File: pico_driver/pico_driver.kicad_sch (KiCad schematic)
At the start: 6 parts, among them J1 GPIO, U1 CAT24C256

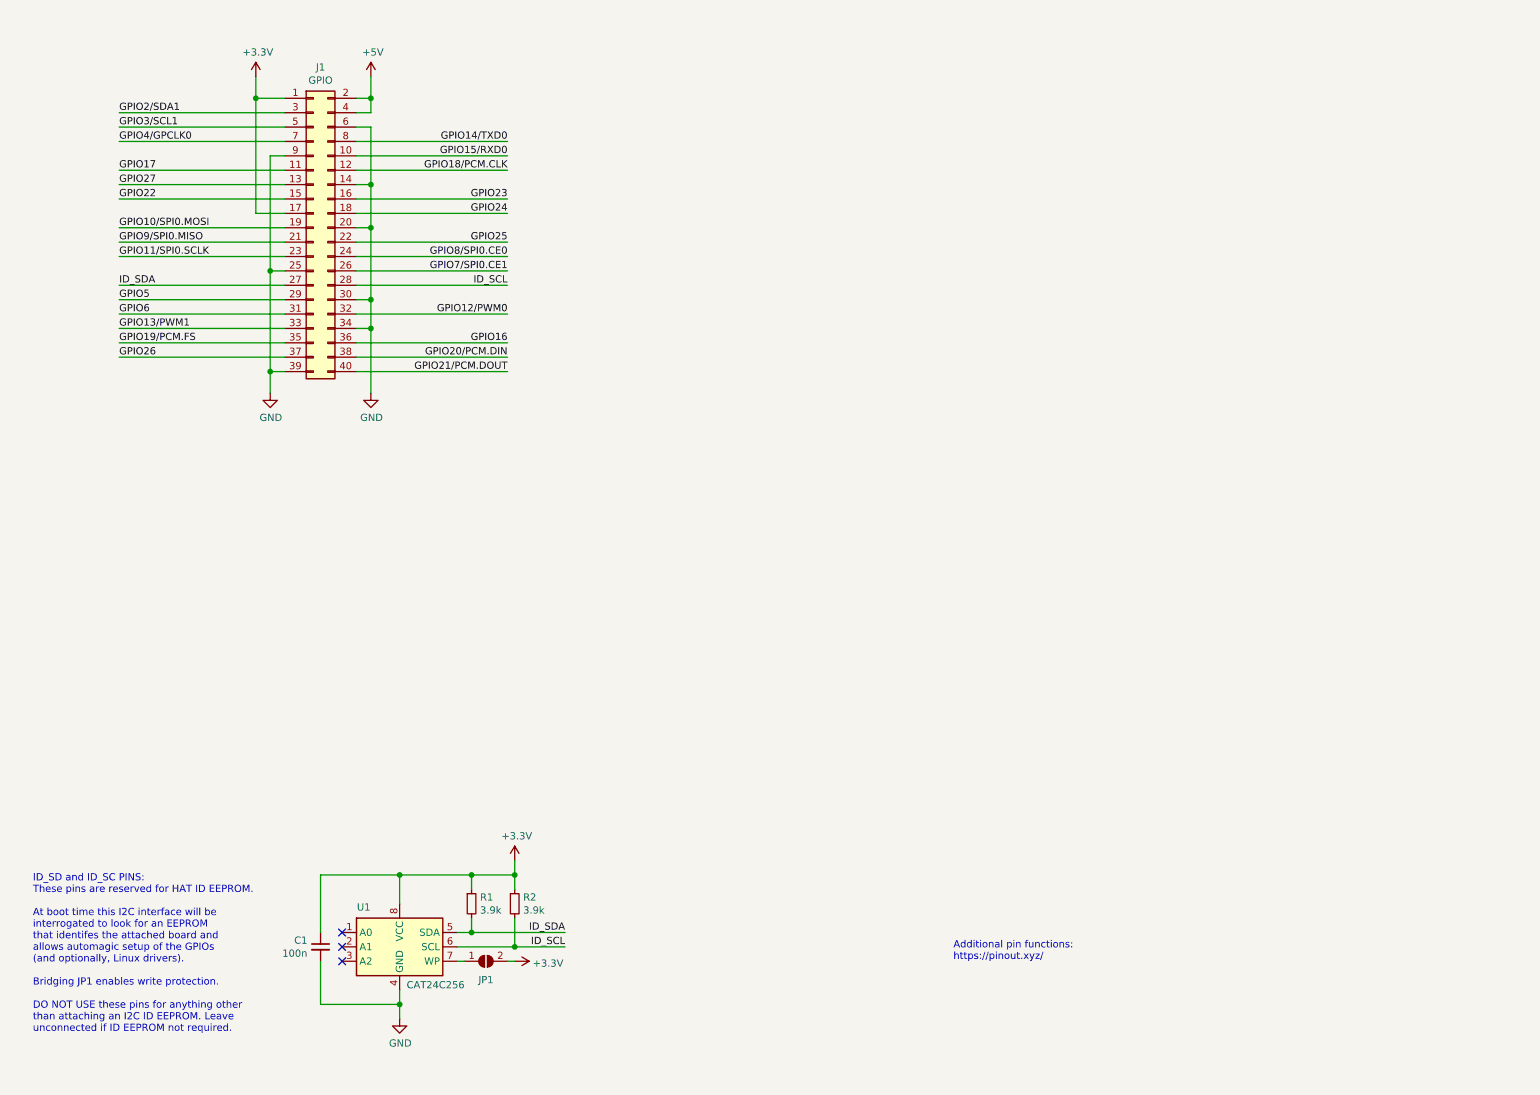
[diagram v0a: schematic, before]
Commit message: update schematic
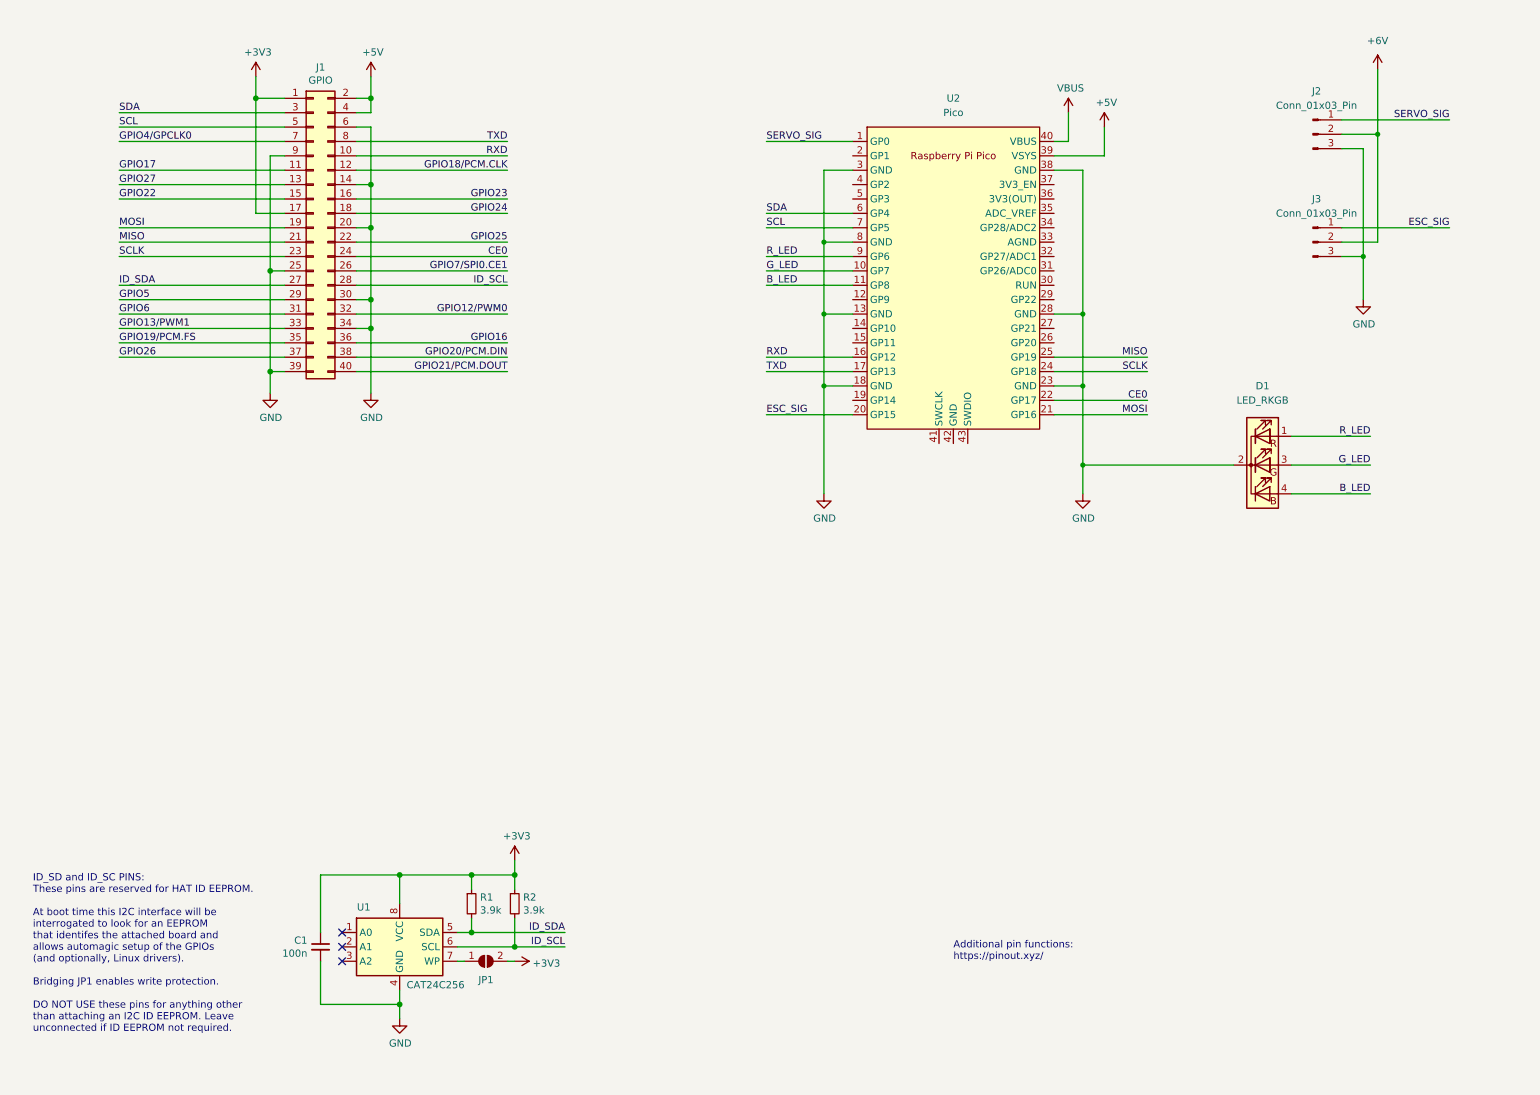
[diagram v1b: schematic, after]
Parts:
- added D1: LED_RKGB, symbol Device:LED_RKGB
- added J2, J3: Conn_01x03_Pin, symbol Connector:Conn_01x03_Pin
- added U2: Pico, RPi_Pico:RPi_Pico_SMD_TH, symbol Pico:Pico
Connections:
- net +5V: now also U2.39 (VSYS)
- net GND: now also D1.2 (K), J2.3 (Pin_3), J3.3 (Pin_3), U2.13 (GND), U2.18 (GND), U2.23 (GND), U2.28 (GND), U2.3 (GND), U2.38 (GND), U2.8 (GND)
- net GPIO10/SPI0.MOSI renamed MOSI
- net MOSI: now also U2.21 (GP16)
- net GPIO11/SPI0.SCLK renamed SCLK
- net SCLK: now also U2.24 (GP18)
- net GPIO14/TXD0 renamed TXD
- net TXD: now also U2.17 (GP13)
- net GPIO15/RXD0 renamed RXD
- net RXD: now also U2.16 (GP12)
- net GPIO2/SDA1 renamed SDA
- net SDA: now also U2.6 (GP4)
- net GPIO3/SCL1 renamed SCL
- net SCL: now also U2.7 (GP5)
- net GPIO8/SPI0.CE0 renamed CE0
- net CE0: now also U2.22 (GP17)
- net GPIO9/SPI0.MISO renamed MISO
- net MISO: now also U2.25 (GP19)
- new net +6V: J2.2 (Pin_2), J3.2 (Pin_2)
- new net B_LED: D1.4 (BA), U2.11 (GP8)
- new net ESC_SIG: J3.1 (Pin_1), U2.20 (GP15)
- new net G_LED: D1.3 (GA), U2.10 (GP7)
- new net R_LED: D1.1 (RA), U2.9 (GP6)
- new net SERVO_SIG: J2.1 (Pin_1), U2.1 (GP0)
- new net VBUS: U2.40 (VBUS)

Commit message: update design
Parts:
- added J4: Conn_01x12_Pin, Connector_PinHeader_2.54mm:PinHeader_1x12_P2.54mm_Vertical, symbol Connector:Conn_01x12_Pin
- added J5: PICO_5VOUT, Connector_PinHeader_2.54mm:PinHeader_1x02_P2.54mm_Vertical, symbol Connector:Conn_01x02_Pin
- added R3, R4, R5: 220R, Resistor_SMD:R_1206_3216Metric_Pad1.30x1.75mm_HandSolder, symbol Device:R
- added SW1: SW_SPDT, Button_Switch_THT:SW_E-Switch_EG1271_SPDT, symbol Switch:SW_SPDT
- added SW2: SW_PU, Button_Switch_THT:SW_PUSH_6mm_H5mm, symbol Switch:SW_SPST
- added SW3: SW_PD, Button_Switch_THT:SW_PUSH_6mm_H5mm, symbol Switch:SW_SPST
- C1: footprint (none) -> Capacitor_SMD:C_0805_2012Metric
- D1: footprint (none) -> LED_THT:LED_D5.0mm-4_RGB
- J2: value Conn_01x03_Pin -> Conn_SERVO; footprint (none) -> Connector_PinHeader_2.54mm:PinHeader_1x03_P2.54mm_Vertical
- J3: value Conn_01x03_Pin -> Conn_ESC; footprint (none) -> Connector_PinHeader_2.54mm:PinHeader_1x03_P2.54mm_Vertical
- JP1: footprint (none) -> Jumper:SolderJumper-2_P1.3mm_Bridged_Pad1.0x1.5mm
- R1, R2: footprint (none) -> Resistor_SMD:R_1206_3216Metric
- U1: footprint (none) -> CAT24C256:TSSOP8_4P50X3P10_ONS
- U2: footprint RPi_Pico:RPi_Pico_SMD_TH -> Pico:RPi_Pico_SMD_TH
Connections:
- net +5V: now also SW1.1 (A); no longer U2.39 (VSYS)
- net B_LED: now also U2.26 (GP20), R5.2; no longer D1.4 (BA), U2.11 (GP8)
- net CE0: now also U2.17 (GP13); no longer U2.22 (GP17)
- net ESC_SIG: now also U2.21 (GP16); no longer U2.20 (GP15)
- net GND: now also U2.33 (AGND), J5.2 (Pin_2), SW3.2 (B)
- net G_LED: now also U2.25 (GP19), R4.2; no longer D1.3 (GA), U2.10 (GP7)
- net MISO: now also U2.15 (GP11); no longer U2.25 (GP19)
- net MOSI: now also U2.16 (GP12); no longer U2.21 (GP16)
- net RXD: now also U2.11 (GP8); no longer U2.16 (GP12)
- net R_LED: now also U2.24 (GP18), R3.2; no longer D1.1 (RA), U2.9 (GP6)
- net SCL: now also U2.20 (GP15); no longer U2.7 (GP5)
- net SCLK: now also U2.14 (GP10); no longer U2.24 (GP18)
- net SDA: now also U2.19 (GP14); no longer U2.6 (GP4)
- net SERVO_SIG: now also U2.27 (GP21); no longer U2.1 (GP0)
- net TXD: now also U2.12 (GP9); no longer U2.17 (GP13)
- net VBUS: now also J5.1 (Pin_1)
- net GP1: now reaches U2.2 (GP1)
- net GP1: now also J4.2 (Pin_2)
- net GP22: now reaches U2.29 (GP22)
- net GP22: now also J4.10 (Pin_10)
- net at U2.31 (GP26/ADC0): now also SW2.1 (A)
- net at U2.32 (GP27/ADC1): now also SW3.1 (A)
- net GP28: now reaches U2.34 (GP28/ADC2)
- net GP28: now also J4.11 (Pin_11)
- net ADC_VREF: now reaches U2.35 (ADC_VREF)
- net ADC_VREF: now also J4.12 (Pin_12)
- net +3V3_PICO: now reaches U2.36 (3V3(OUT))
- net +3V3_PICO: now also SW2.2 (B)
- net GP2: now reaches U2.4 (GP2)
- net GP2: now also J4.3 (Pin_3)
- net GP3: now reaches U2.5 (GP3)
- net GP3: now also J4.4 (Pin_4)
- net +6V renamed VBEC
- new net: D1.4 (BA), R5.1
- new net: D1.3 (GA), R4.1
- new net: D1.1 (RA), R3.1
- new net GP0: J4.1 (Pin_1), U2.1 (GP0)
- new net GP17: J4.9 (Pin_9), U2.22 (GP17)
- new net GP4: J4.5 (Pin_5), U2.6 (GP4)
- new net GP5: J4.6 (Pin_6), U2.7 (GP5)
- new net GP6: J4.7 (Pin_7), U2.9 (GP6)
- new net GP7: J4.8 (Pin_8), U2.10 (GP7)
- new net VSYS: SW1.2 (B), U2.39 (VSYS)
- no-connect marks 3 -> 7
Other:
- moved on the sheet: J2, J3

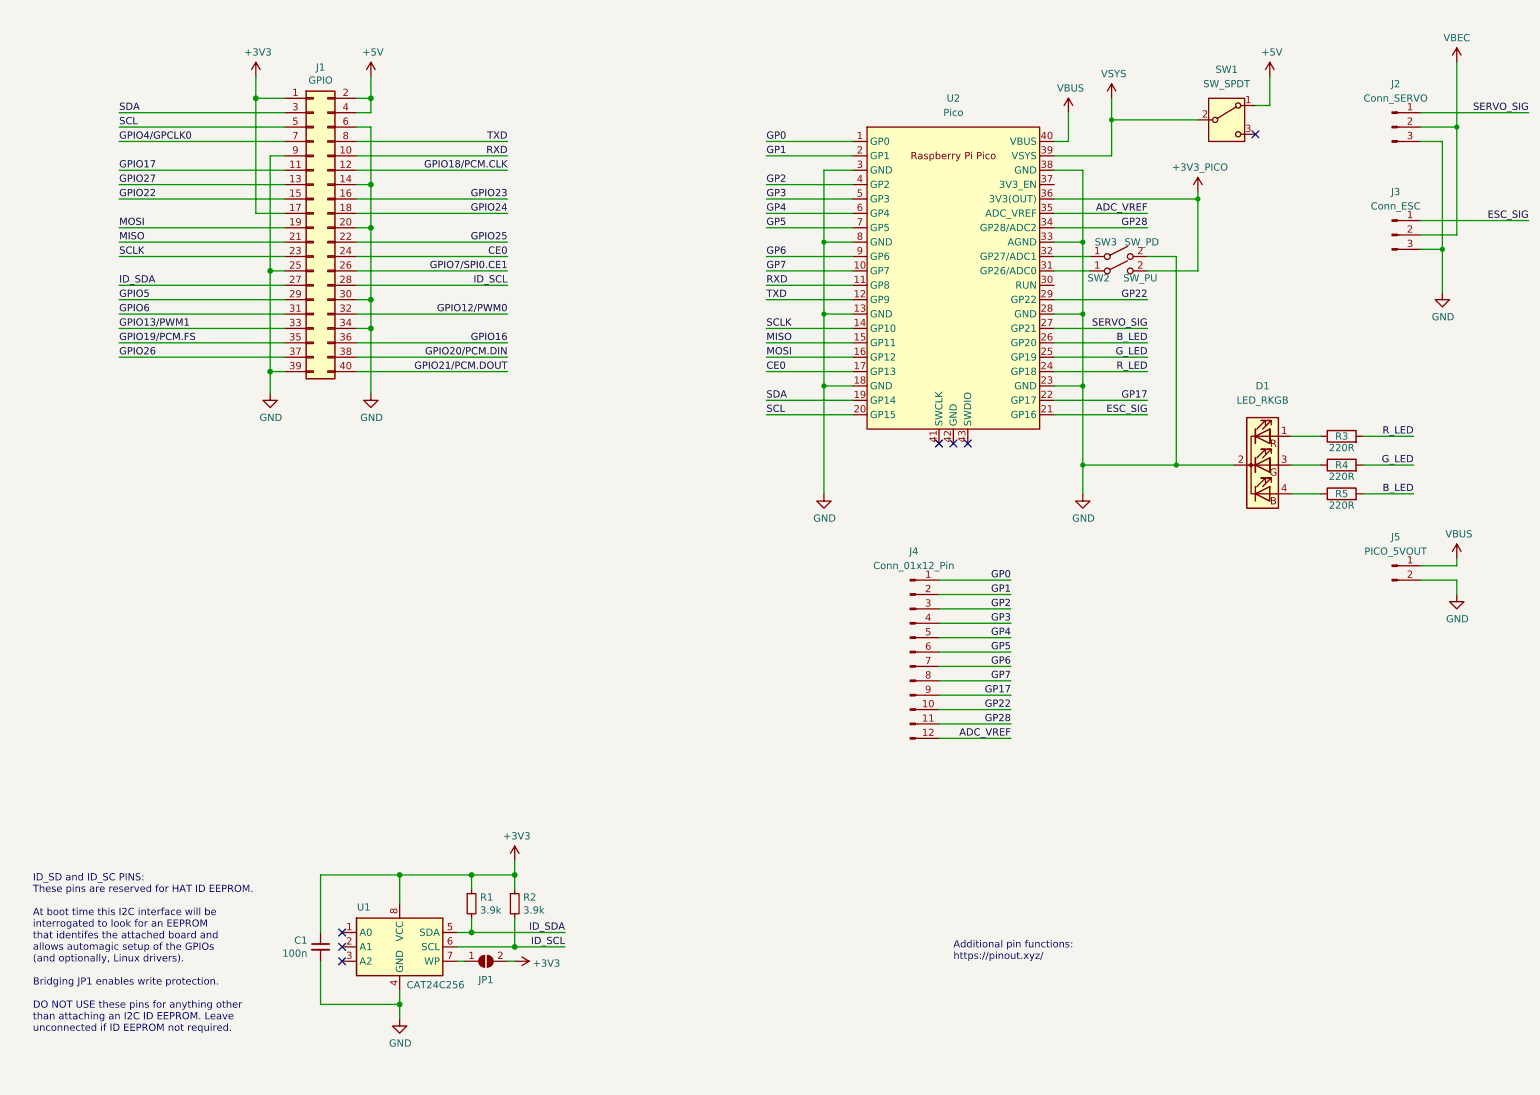
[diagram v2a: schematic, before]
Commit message: update design
1. paralleled capacitor to debounce buttons
2. rewired
3. generated gerbers
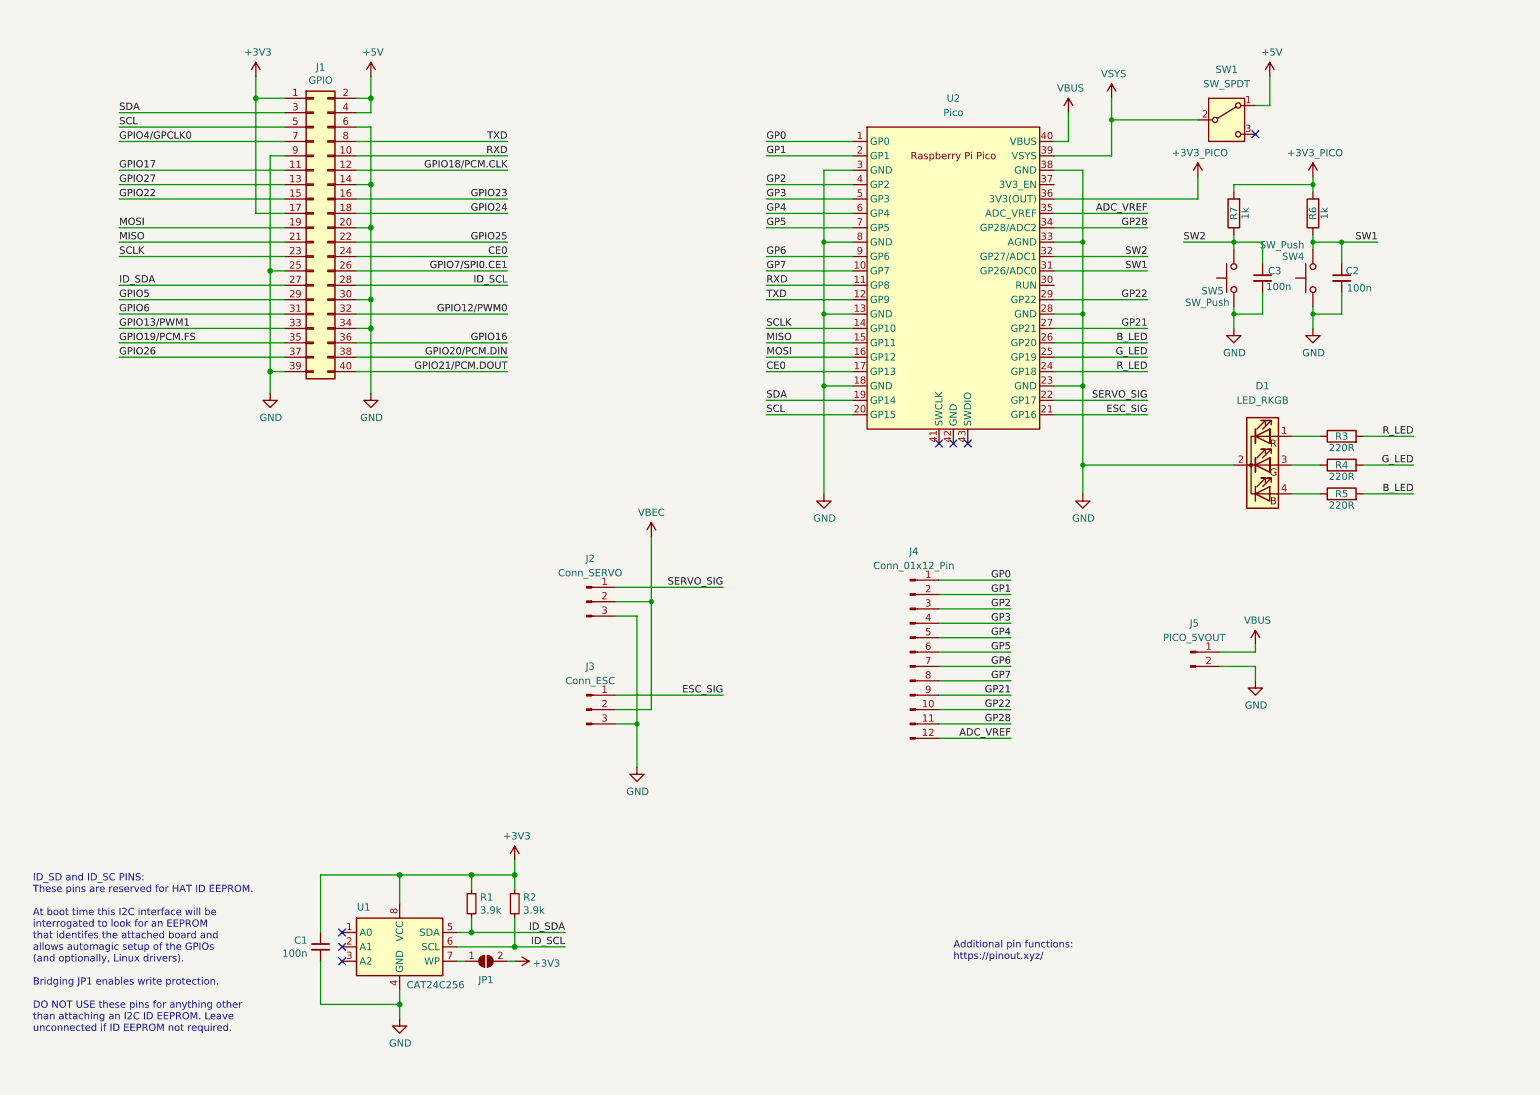
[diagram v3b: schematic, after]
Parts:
- removed SW2: SW_PU, Button_Switch_THT:SW_PUSH_6mm_H5mm, symbol Switch:SW_SPST
- removed SW3: SW_PD, Button_Switch_THT:SW_PUSH_6mm_H5mm, symbol Switch:SW_SPST
- added C2, C3: 100n, Capacitor_SMD:C_0805_2012Metric, symbol Device:C_Small
- added R6, R7: 1k, Resistor_SMD:R_1206_3216Metric_Pad1.30x1.75mm_HandSolder, symbol Device:R
- added SW4, SW5: SW_Push, Button_Switch_THT:SW_PUSH_6mm_H5mm, symbol Switch:SW_Push
- D1: footprint LED_THT:LED_D5.0mm-4_RGB -> LED_THT:LED_D5.0mm-4_RGB_Wide_Pins
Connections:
- net +3V3_PICO: now also R6.2, R7.2
- net GND: now also C2.2, C3.2, SW4.1, SW5.1
- net SERVO_SIG: now also U2.22 (GP17); no longer U2.27 (GP21)
- net SW1: now reaches U2.31 (GP26/ADC0)
- net SW1: now also C2.1, R6.1, SW4.2
- net SW2: now reaches U2.32 (GP27/ADC1)
- net SW2: now also C3.1, R7.1, SW5.2
- net GP17 renamed GP21
- net GP21: now also U2.27 (GP21); no longer U2.22 (GP17)
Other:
- moved on the sheet: J2, J3, J5

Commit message: export schematic pdf
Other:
- title: (none) -> BearCart - Cerebellum
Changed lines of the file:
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@@
 	(generator "eeschema")
 	(generator_version "9.0")
-	(paper "A4")
+	(paper "USLetter")
 	(title_block
-		(date "15 nov 2012")
+		(title "BearCart - Cerebellum")
+		(date "2025-04-25")
 	)
 	(text "Additional pin functions:\nhttps://pinout.xyz/"
